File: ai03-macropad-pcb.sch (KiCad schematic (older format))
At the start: 15 parts

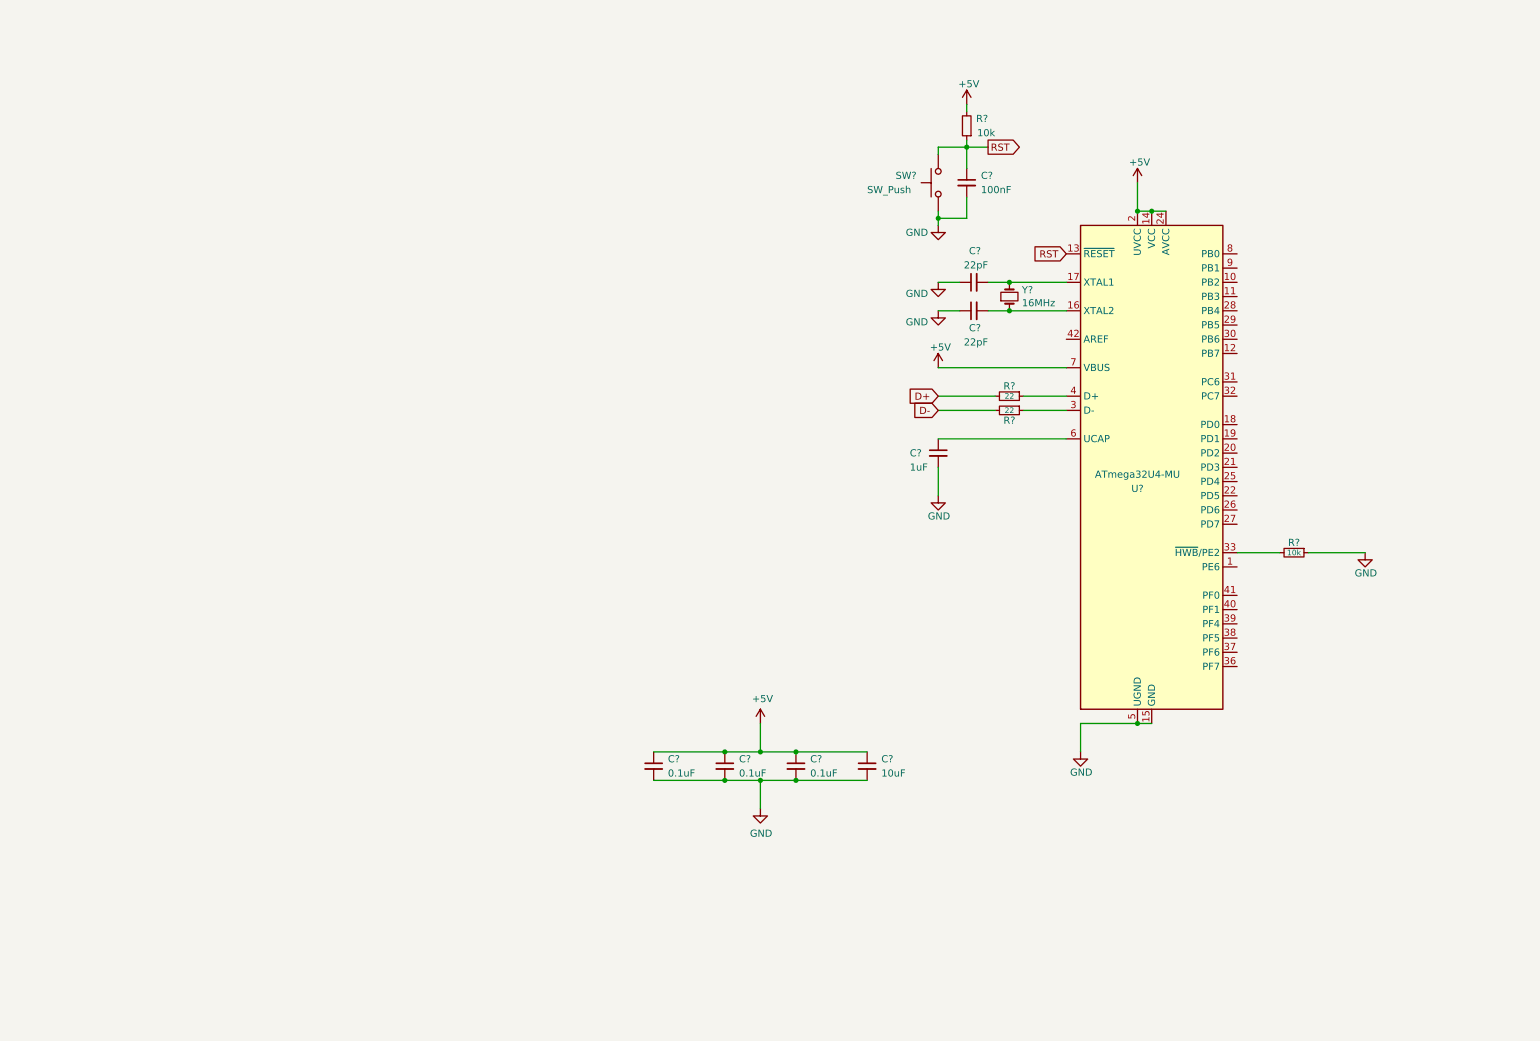
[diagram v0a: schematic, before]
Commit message: USB-C and ESD schematic
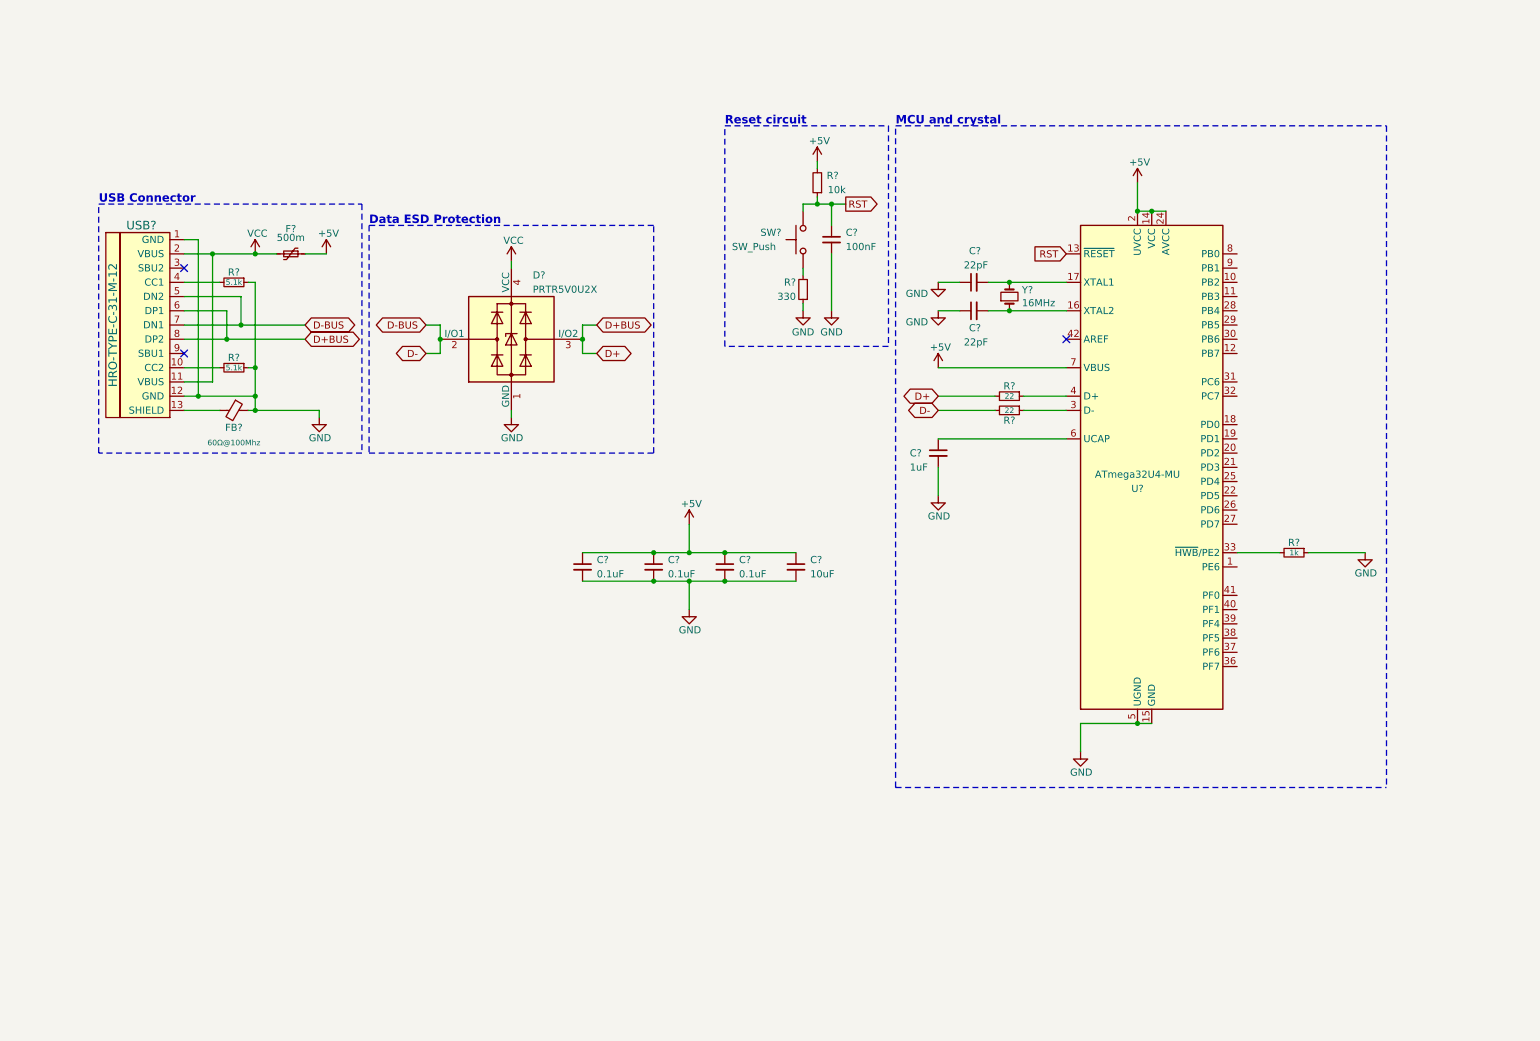
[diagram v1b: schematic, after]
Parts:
- added D?: PRTR5V0U2X, Package_TO_SOT_SMD:SOT-143, symbol Power_Protection:PRTR5V0U2X
- added F?: 500m, symbol Device:Polyfuse_Small
- added FB?: 60Ω@100Mhz, symbol Device:Ferrite_Bead_Small
- added R?: 330, symbol Device:R_Small
- added R? (x2): 5.1k, symbol Device:R_Small
- added USB?: HRO-TYPE-C-31-M-12, symbol Type-C:HRO-TYPE-C-31-M-12
- R?: value 10k -> 1k
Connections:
- net +5V: now also F?.1
- net D+: now also D?.3 (I/O2), USB?.6 (DP1), USB?.8 (DP2)
- net D-: now also D?.2 (I/O1), USB?.5 (DN2), USB?.7 (DN1)
- net GND: now also D?.1 (GND), FB?.1, R?.1, R?.1, R?.1, USB?.1 (GND), USB?.12 (GND); no longer SW?.1
- new net: R?.2, USB?.10 (CC2)
- new net: FB?.2, USB?.13 (SHIELD)
- new net: R?.2, USB?.4 (CC1)
- new net: R?.2, SW?.1
- new net VCC: D?.4 (VCC), F?.2, USB?.11 (VBUS), USB?.2 (VBUS)
- no-connect marks 0 -> 3
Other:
- note added: "Data ESD Protection"
- note added: "MCU and crystal"
- note added: "Reset circuit"
- note added: "USB Connector"
- moved on the sheet: C?, R?, SW?

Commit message: Switch matrix and RGB array
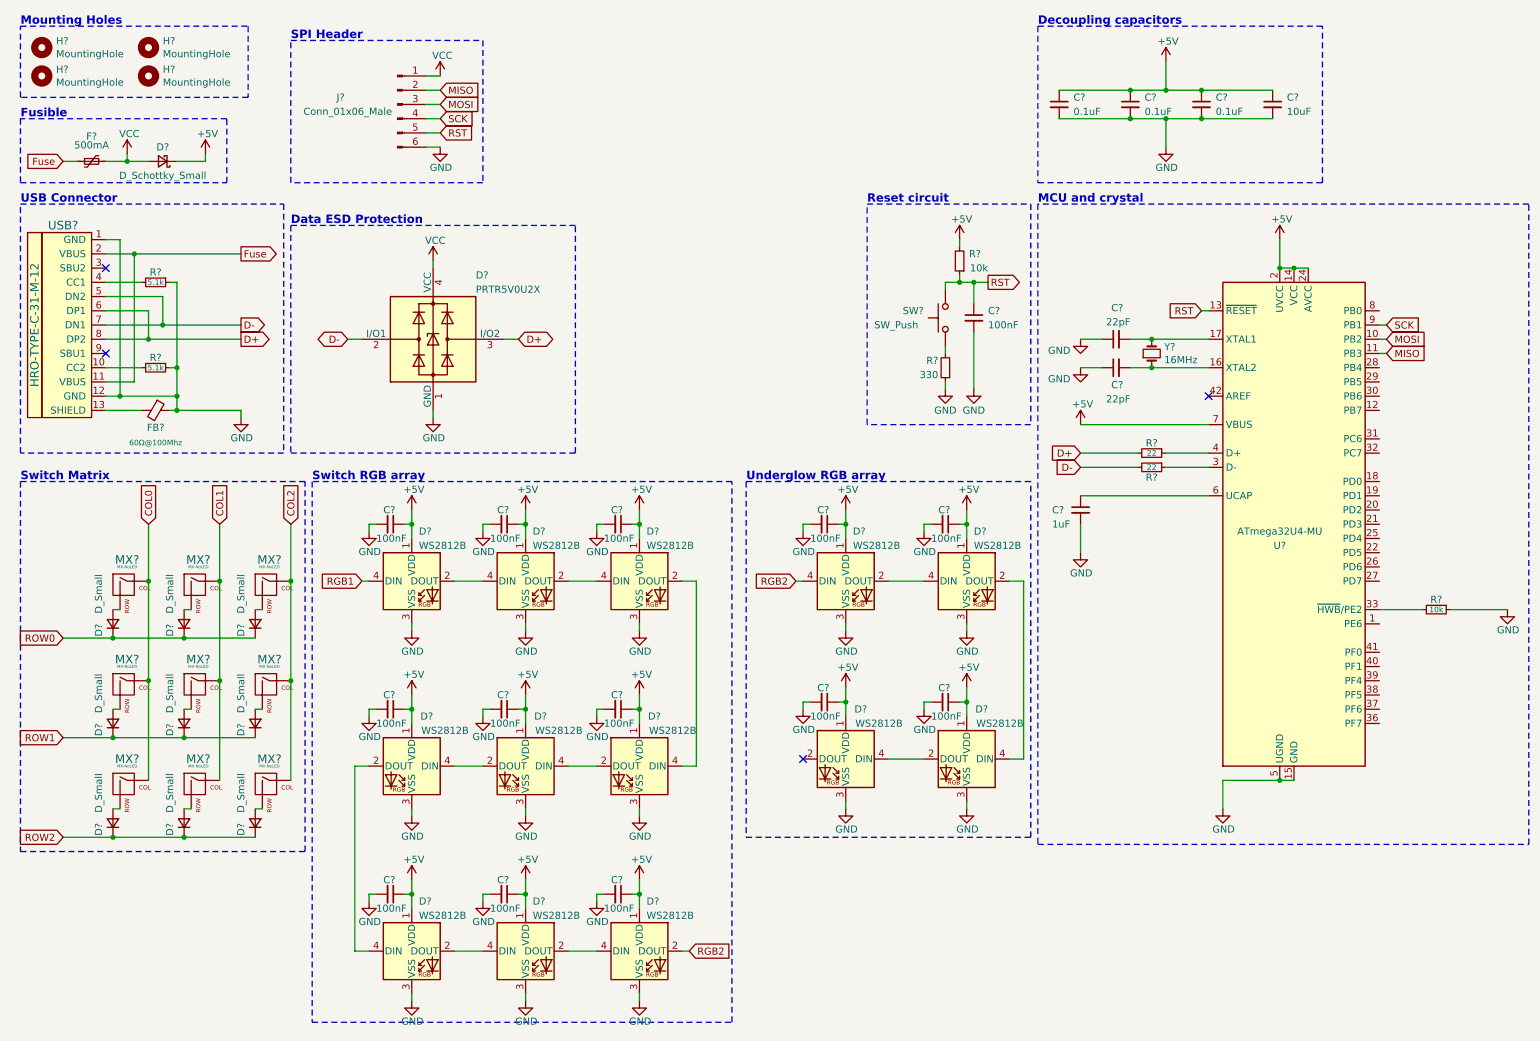
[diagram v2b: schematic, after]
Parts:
- added C? (x13): 100nF, symbol Device:C_Small
- added D? (x9): D_Small, symbol Device:D_Small
- added D?: D_Schottky_Small, symbol Device:D_Schottky_Small
- added D? (x13): WS2812B, LED_SMD:LED_WS2812B_PLCC4_5.0x5.0mm_P3.2mm, symbol LED:WS2812B
- added H? (x4): MountingHole, symbol Mechanical:MountingHole
- added J?: Conn_01x06_Male, symbol Connector:Conn_01x06_Male
- added MX? (x9): MX-NoLED, symbol MX_Alps_Hybrid:MX-NoLED
- F?: value 500m -> 500mA
- R?: value 1k -> 10k
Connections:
- net +5V: now also C?.1, C?.1, C?.1, C?.1, C?.1, C?.1, C?.1, C?.1, C?.1, C?.1, C?.1, C?.1, C?.1, D?.1 (K), D?.1 (VDD), D?.1 (VDD), D?.1 (VDD), D?.1 (VDD), D?.1 (VDD), D?.1 (VDD), D?.1 (VDD), D?.1 (VDD), D?.1 (VDD), D?.1 (VDD), D?.1 (VDD), D?.1 (VDD), D?.1 (VDD); no longer F?.1
- net GND: now also C?.2, C?.2, C?.2, C?.2, C?.2, C?.2, C?.2, C?.2, C?.2, C?.2, C?.2, C?.2, C?.2, D?.3 (VSS), D?.3 (VSS), D?.3 (VSS), D?.3 (VSS), D?.3 (VSS), D?.3 (VSS), D?.3 (VSS), D?.3 (VSS), D?.3 (VSS), D?.3 (VSS), D?.3 (VSS), D?.3 (VSS), D?.3 (VSS), J?.6 (Pin_6)
- net RST: now also J?.5 (Pin_5)
- net VCC: now also F?.1, D?.2 (A), J?.1 (Pin_1); no longer F?.2, USB?.11 (VBUS), USB?.2 (VBUS)
- net MOSI: now reaches U?.10 (PB2)
- net MOSI: now also J?.3 (Pin_3)
- net MISO: now reaches U?.11 (PB3)
- net MISO: now also J?.2 (Pin_2)
- net SCK: now reaches U?.9 (PB1)
- net SCK: now also J?.4 (Pin_4)
- new net: D?.2 (A), MX?.2 (ROW) (x9)
- new net: D?.2 (DOUT), D?.4 (DIN) (x11)
- new net COL0: MX?.1 (COL), MX?.1 (COL), MX?.1 (COL)
- new net COL1: MX?.1 (COL), MX?.1 (COL), MX?.1 (COL)
- new net COL2: MX?.1 (COL), MX?.1 (COL), MX?.1 (COL)
- new net Fuse: F?.2, USB?.11 (VBUS), USB?.2 (VBUS)
- new net RGB1: D?.4 (DIN)
- new net RGB2: D?.2 (DOUT), D?.4 (DIN)
- new net ROW0: D?.1 (K), D?.1 (K), D?.1 (K)
- new net ROW1: D?.1 (K), D?.1 (K), D?.1 (K)
- new net ROW2: D?.1 (K), D?.1 (K), D?.1 (K)
- no-connect marks 3 -> 4
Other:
- note added: "Decoupling capacitors"
- note added: "Fusible"
- note added: "Mounting Holes"
- note added: "SPI Header"
- note added: "Switch Matrix"
- note added: "Switch RGB array"
- note added: "Underglow RGB array"
- moved on the sheet: C?, D?, F?, FB?, R?, SW?, U?, USB?, Y?

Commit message: Footprints and schematic fixes
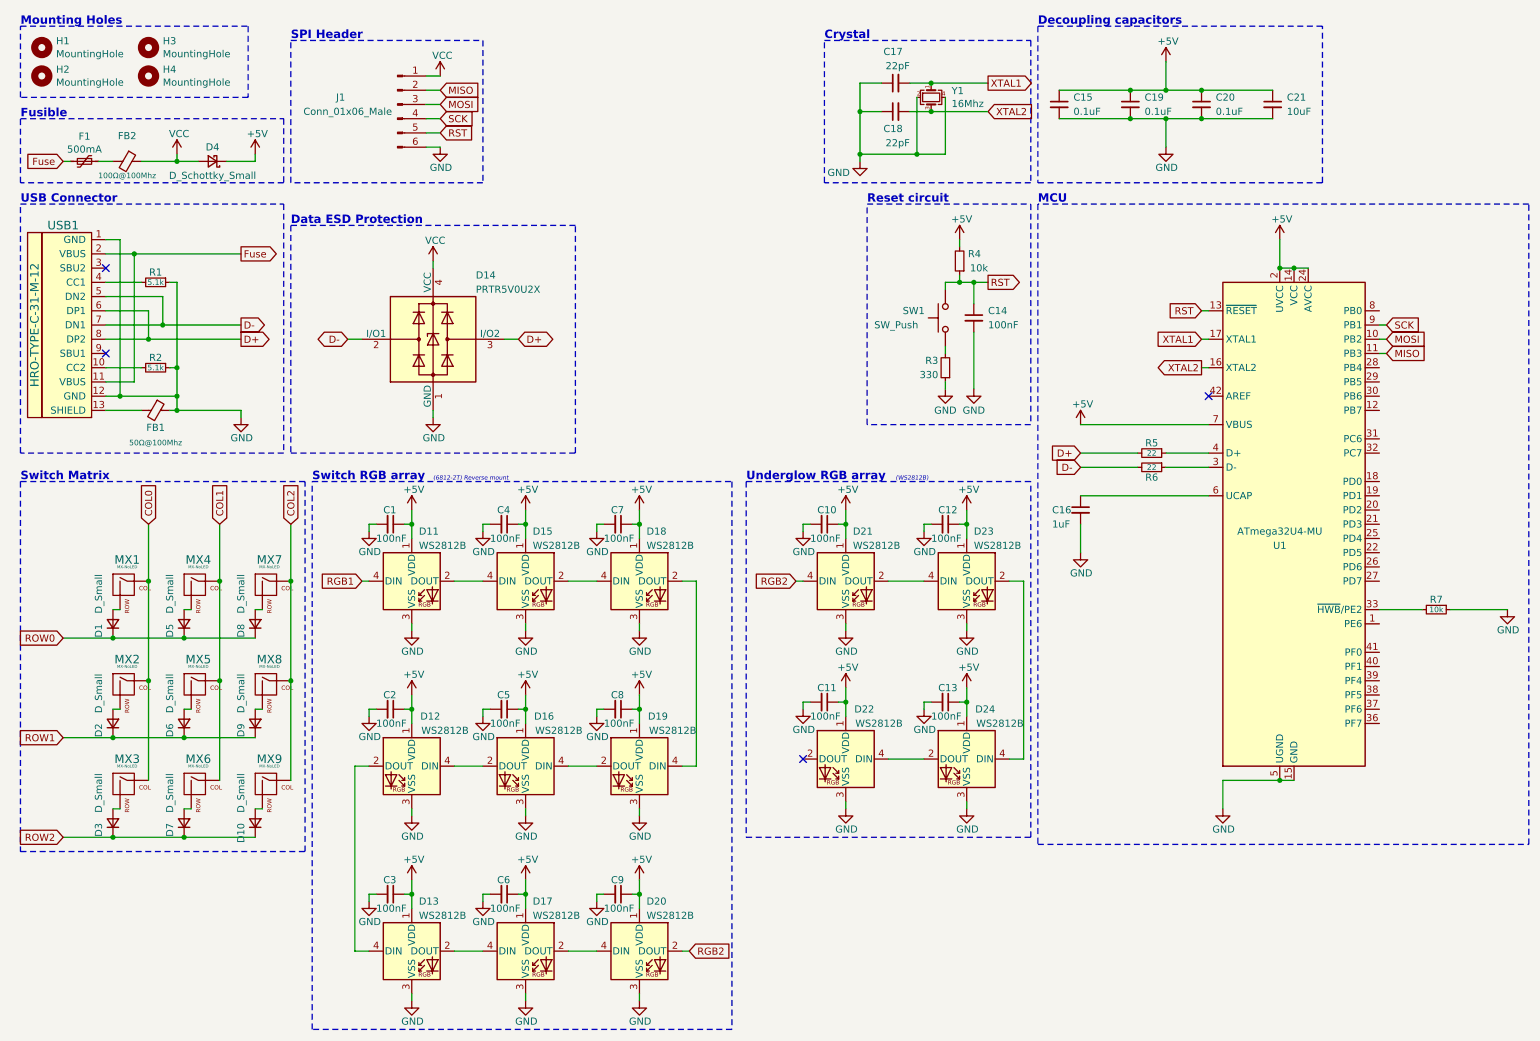
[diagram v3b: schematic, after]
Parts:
- removed Y?: 16MHz, symbol Device:Crystal_Small
- added FB2: 100Ω@100Mhz, Fuse:Fuse_0805_2012Metric, symbol Device:Ferrite_Bead_Small
- added Y1: 16Mhz, Crystal:Crystal_SMD_3225-4Pin_3.2x2.5mm, symbol Device:Crystal_GND24_Small
- C1, C10, C11, C12, C13, C14, C15, C16, C17, C18, C19, C2, C20, C21, C3, C4, C5, C6, C7, C8, C9: renamed from C?; footprint (none) -> Capacitor_SMD:C_0603_1608Metric
- D1, D10, D2, D3, D4, D5, D6, D7, D8, D9: renamed from D?; footprint (none) -> Diode_SMD:D_SOD-123
- F1: renamed from F?; footprint (none) -> Fuse:Fuse_0805_2012Metric
- FB1: renamed from FB?; value 60Ω@100Mhz -> 50Ω@100Mhz; footprint (none) -> Fuse:Fuse_0603_1608Metric
- H1, H2, H3, H4: renamed from H?; footprint (none) -> MountingHole:MountingHole_3.2mm_M3_Pad_TopBottom
- MX1, MX2, MX3, MX4, MX5, MX6, MX7, MX8, MX9: renamed from MX?; footprint (none) -> MX_Only:MXOnly-1U-Hotswap-Antishear
- R1, R2, R3, R4, R5, R6, R7: renamed from R?; footprint (none) -> Resistor_SMD:R_0603_1608Metric
- SW1: renamed from SW?; footprint (none) -> random-keyboard-parts:SKQG-1155865
- USB1: renamed from USB?; footprint (none) -> Type-C:HRO-TYPE-C-31-M-12-Assembly
- gave numbers to parts that had none: 16
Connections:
- net GND: now also Y1.2, Y1.4
- net VCC: now also FB2.1; no longer F1.1
- net XTAL2: now reaches C18.2, U1.16 (XTAL2)
- net XTAL2: now also Y1.3
- net XTAL1: now reaches C17.2, U1.17 (XTAL1)
- net XTAL1: now also Y1.1
- new net: F1.1, FB2.2
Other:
- note added: "(6812-2T) Reverse mount"
- note added: "(WS2812B)"
- note added: "Crystal"
- note added: "MCU"
- note removed: "MCU and crystal"
- moved on the sheet: C17, C18, D4, F1

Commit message: Schematic improvements and added libraries
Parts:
- removed D11, D12, D13, D15, D16, D17, D18, D19, D20, D21, D22, D23, D24: WS2812B, LED_SMD:LED_WS2812B_PLCC4_5.0x5.0mm_P3.2mm, symbol LED:WS2812B
- removed J1: Conn_01x06_Male, symbol Connector:Conn_01x06_Male
- added D11, D12, D13, D15, D16, D17, D18, D19, D20: SK6812MINI-E, kicad-keyboard-parts:MX_SK6812MINI-E, symbol kicad-keyboard-parts:SK6812MINI-E
- added D21, D22, D23, D24: WS2812B-MINI, LED_SMD:LED_SK6812MINI_PLCC4_3.5x3.5mm_P1.75mm, symbol kicad-keyboard-parts:WS2812B-MINI
- added J1: Conn_01x06, Connector_JST:JST_SH_BM06B-SRSS-TB_1x06-1MP_P1.00mm_Vertical, symbol Connector_Generic:Conn_01x06
- added R8: 300, Resistor_SMD:R_0603_1608Metric, symbol Device:R_Small
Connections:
- net +5V: now also D11.1 (VDD), D12.1 (VDD), D13.1 (VDD), D15.1 (VDD), D16.1 (VDD), D17.1 (VDD), D18.1 (VDD), D19.1 (VDD), D20.1 (VDD), D21.1 (VDD), D22.1 (VDD), D23.1 (VDD), D24.1 (VDD)
- net GND: now also D11.3 (VSS), D12.3 (VSS), D13.3 (VSS), D15.3 (VSS), D16.3 (VSS), D17.3 (VSS), D18.3 (VSS), D19.3 (VSS), D20.3 (VSS), D21.3 (VSS), D22.3 (VSS), D23.3 (VSS), D24.3 (VSS), J1.1 (Pin_1)
- net MISO: now also J1.2 (Pin_2)
- net MOSI: now also J1.3 (Pin_3)
- net RGB1: now also D11.4 (DIN), R8.1
- net RGB2: now also D20.2 (DOUT), D21.4 (DIN)
- net RST: now also J1.5 (Pin_5)
- net SCK: now also J1.4 (Pin_4)
- net VCC: now also J1.6 (Pin_6)
- new net: D11.2 (DOUT), D15.4 (DIN)
- new net: D15.2 (DOUT), D18.4 (DIN)
- new net: D18.2 (DOUT), D19.4 (DIN)
- new net: D16.4 (DIN), D19.2 (DOUT)
- new net: D12.4 (DIN), D16.2 (DOUT)
- new net: D12.2 (DOUT), D13.4 (DIN)
- new net: D13.2 (DOUT), D17.4 (DIN)
- new net: D17.2 (DOUT), D20.4 (DIN)
- new net: D21.2 (DOUT), D23.4 (DIN)
- new net: D23.2 (DOUT), D24.4 (DIN)
- new net: D22.4 (DIN), D24.2 (DOUT)
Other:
- note added: "303-another-macrobad"
- note added: "A"
- note added: "April 2021"
- moved on the sheet: C10, C11, C12, C13
